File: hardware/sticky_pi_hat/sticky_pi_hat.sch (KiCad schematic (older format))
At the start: 28 parts, among them J1 Screw_Terminal_01x11, J2 Conn_02x13_Odd_Even, J3 Conn_01x02_Male, Q1 BSS806NH6327XTSA1, SW1 SW_Push, U1 DHT22, U2 TPL5110, U3 TPS63002, U4 DS1307Z+, Y1 Crystal

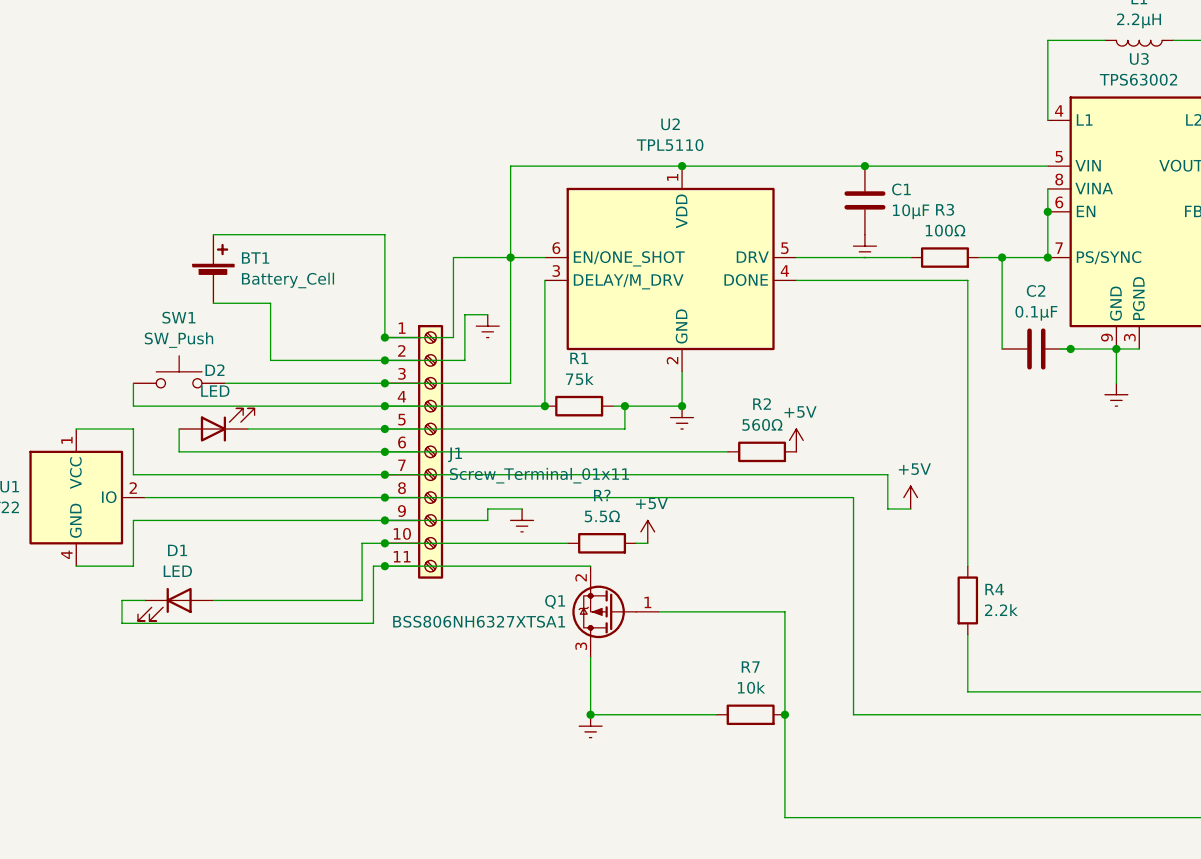
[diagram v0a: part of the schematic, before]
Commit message: Add P-channel mosfet to tpl5110
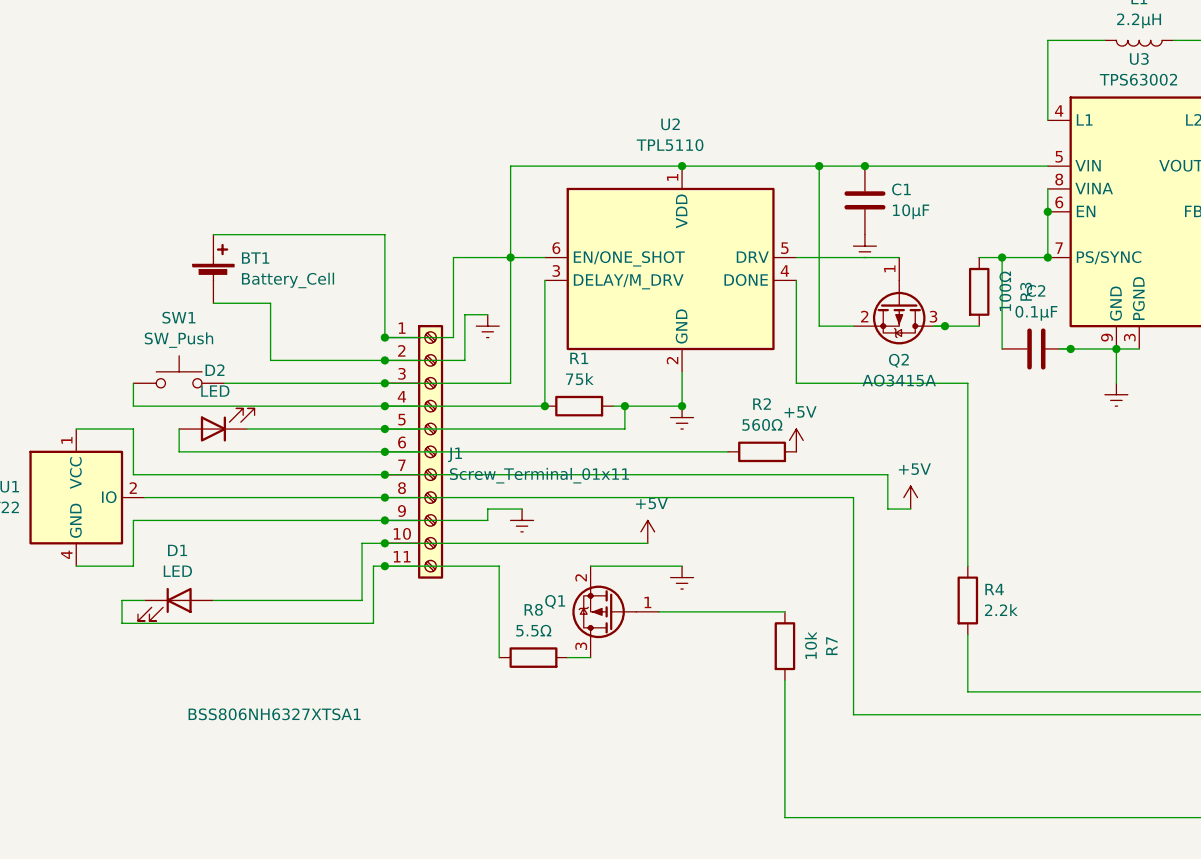
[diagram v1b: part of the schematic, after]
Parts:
- added Q2: AO3415A, Package_TO_SOT_SMD:SOT-23, symbol Transistor_FET:BSS84
- Q1: part_number SI2319CDS-T1-GE3 -> BSS806NH6327XTSA1
- gave numbers to parts that had none: 1
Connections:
- wire segments 129 -> 134
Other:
- moved on the sheet: R3, R7, R8
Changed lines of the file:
@@
 L Device:R R3
 U 1 1 613829B2
-P 5450 2650
-F 0 "R3" V 5657 2650 50  0000 C CNN
-F 1 "100Ω" V 5566 2650 50  0000 C CNN
-F 2 "Resistor_SMD:R_2010_5025Metric" V 5380 2650 50  0001 C CNN
-F 3 "https://www.koaspeer.com/pdfs/RK73H.pdf" H 5450 2650 50  0001 C CNN
-F 4 "RC2010JK-0710KL" H 5450 2650 50  0001 C CNN "part_number"
-F 5 "KOA Speer Electronics, Inc." H 5450 2650 50  0001 C CNN "Manufacturer"
-F 6 "" H 5450 2650 50  0001 C CNN "Vendor"
-F 7 "RC2010JK-0710KL" H 5450 2650 50  0001 C CNN "Part"
-	1    5450 2650
-	0    -1   -1   0
+P 5600 2800
+F 0 "R3" V 5807 2800 50  0000 C CNN
+F 1 "100Ω" V 5716 2800 50  0000 C CNN
+F 2 "Resistor_SMD:R_2010_5025Metric" V 5530 2800 50  0001 C CNN
+F 3 "https://www.koaspeer.com/pdfs/RK73H.pdf" H 5600 2800 50  0001 C CNN
+F 4 "RC2010JK-0710KL" H 5600 2800 50  0001 C CNN "part_number"
+F 5 "KOA Speer Electronics, Inc." H 5600 2800 50  0001 C CNN "Manufacturer"
+F 6 "" H 5600 2800 50  0001 C CNN "Vendor"
+F 7 "RC2010JK-0710KL" H 5600 2800 50  0001 C CNN "Part"
+	1    5600 2800
+	1    0    0    -1
 $EndComp
 $Comp
@@
 	1    0    0    -1
 $EndComp
-$Comp
-L Device:C C1
-U 1 1 613C0503
-P 5100 2400
-F 0 "C1" H 5215 2446 50  0000 L CNN
-F 1 "10μF" H 5215 2355 50  0000 L CNN
-F 2 "Capacitor_SMD:C_1206_3216Metric" H 5138 2250 50  0001 C CNN
-F 3 "https://global.kyocera.com/prdct/electro/product/pdf/cm_e.pdf" H 5100 2400 50  0001 C CNN
-F 4 "CM316X5R106K10AT" H 5100 2400 50  0001 C CNN "part_number"
-F 5 "Kyocera International Inc. Electronic Components" H 5100 2400 50  0001 C CNN "Manufacturer"
-F 6 "" H 5100 2400 50  0001 C CNN "Vendor"
-F 7 "CM316X5R106K10AT" H 5100 2400 50  0001 C CNN "Part"
-	1    5100 2400
-	1    0    0    -1
-$EndComp
 Wire Wire Line
 	5600 2650 5700 2650
@@
 Wire Wire Line
 	6000 3050 6200 3050
-$Comp
-L power:Earth #PWR0103
-U 1 1 613C9F6B
-P 5100 2550
-F 0 "#PWR0103" H 5100 2300 50  0001 C CNN
-F 1 "Earth" H 5100 2400 50  0001 C CNN
-F 2 "" H 5100 2550 50  0001 C CNN
-F 3 "~" H 5100 2550 50  0001 C CNN
-	1    5100 2550
-	1    0    0    -1
-$EndComp
 Wire Wire Line
 	6700 2450 6700 2250
@@
 	1    0    0    -1
 $EndComp
-Wire Wire Line
-	3000 4000 3900 4000
 $Comp
 L power:Earth #PWR0108
 U 1 1 615E52C8
-P 3900 4650
-F 0 "#PWR0108" H 3900 4400 50  0001 C CNN
-F 1 "Earth" H 3900 4500 50  0001 C CNN
-F 2 "" H 3900 4650 50  0001 C CNN
-F 3 "~" H 3900 4650 50  0001 C CNN
-	1    3900 4650
+P 4300 4000
+F 0 "#PWR0108" H 4300 3750 50  0001 C CNN
+F 1 "Earth" H 4300 3850 50  0001 C CNN
+F 2 "" H 4300 4000 50  0001 C CNN
+F 3 "~" H 4300 4000 50  0001 C CNN
+	1    4300 4000
 	1    0    0    -1
 $EndComp
@@
 	7250 2250 7300 2250
 Wire Wire Line
-	4750 4650 4750 4200
-Wire Wire Line
 	3000 4000 2950 4000
-Connection ~ 3000 4000
 Wire Wire Line
 	3000 3900 2900 3900
-Connection ~ 3000 3900
 Wire Wire Line
 	3000 3700 5050 3700
@@
 P 4000 4200
 F 0 "Q1" H 4205 4154 50  0000 L CNN
-F 1 "BSS806NH6327XTSA1" H 4205 4245 50  0000 L CNN
+F 1 "BSS806NH6327XTSA1" H 5100 4650 50  0000 L CNN
 F 2 "Package_TO_SOT_SMD:SOT-23" H 4200 4125 50  0001 L CIN
 F 3 "https://www.infineon.com/dgdl/BSS806N_Rev2.3_.pdf?folderId=db3a3043156fd573011622e10b5c1f67&fileId=db3a304330f686060131185f0553451c" H 4000 4200 50  0001 L CNN
 F 4 "Infineon Technologies" H 4000 4200 50  0001 C CNN "Manufacturer"
-F 5 "SI2319CDS-T1-GE3" H 4000 4200 50  0001 C CNN "part_number"
+F 5 "BSS806NH6327XTSA1" H 4000 4200 50  0001 C CNN "part_number"
 F 6 "" H 4000 4200 50  0001 C CNN "Vendor"
 F 7 "BSS806NH6327XTSA1" H 4000 4200 50  0001 C CNN "Part"
@@
 L Device:R R7
 U 1 1 61A13B53
-P 4600 4650
-F 0 "R7" V 4807 4650 50  0000 C CNN
-F 1 "10k" V 4716 4650 50  0000 C CNN
-F 2 "Resistor_SMD:R_2010_5025Metric" V 4530 4650 50  0001 C CNN
-F 3 "https://www.yageo.com/upload/media/product/productsearch/datasheet/rchip/PYu-RC_Group_51_RoHS_L_11.pdf" H 4600 4650 50  0001 C CNN
-F 4 "RC2010JK-0710KL" H 4600 4650 50  0001 C CNN "part_number"
-F 5 "YAGEO" H 4600 4650 50  0001 C CNN "Manufacturer"
-F 6 "" H 4600 4650 50  0001 C CNN "Vendor"
-F 7 "RC2010JK-0710KL" H 4600 4650 50  0001 C CNN "Part"
-	1    4600 4650
-	0    -1   -1   0
+P 4750 4350
+F 0 "R7" V 4957 4350 50  0000 C CNN
+F 1 "10k" V 4866 4350 50  0000 C CNN
+F 2 "Resistor_SMD:R_2010_5025Metric" V 4680 4350 50  0001 C CNN
+F 3 "https://www.yageo.com/upload/media/product/productsearch/datasheet/rchip/PYu-RC_Group_51_RoHS_L_11.pdf" H 4750 4350 50  0001 C CNN
+F 4 "RC2010JK-0710KL" H 4750 4350 50  0001 C CNN "part_number"
+F 5 "YAGEO" H 4750 4350 50  0001 C CNN "Manufacturer"
+F 6 "" H 4750 4350 50  0001 C CNN "Vendor"
+F 7 "RC2010JK-0710KL" H 4750 4350 50  0001 C CNN "Part"
+	1    4750 4350
+	1    0    0    -1
 $EndComp
 Wire Wire Line
 	4750 4200 4200 4200
 Wire Wire Line
-	3900 4400 3900 4650
-Wire Wire Line
-	4450 4650 3900 4650
-Connection ~ 3900 4650
-Wire Wire Line
 	7900 4150 7900 4250
 Wire Wire Line
@@
 Wire Wire Line
 	5050 3700 5050 4650
-Wire Wire Line
-	4750 5100 4750 4650
-Connection ~ 4750 4650
 Connection ~ 5100 2250
-Wire Wire Line
-	5100 2250 4300 2250
-Wire Wire Line
-	4800 2650 5300 2650
 $Comp
 L power:+5V #PWR0113
@@
 	1    0    0    -1
 $EndComp
-Wire Wire Line
-	5550 2750 4800 2750
-Wire Wire Line
-	5550 2750 5550 4000
 Wire Wire Line
 	8100 3500 8100 4050
@@
 	7950 4650 5050 4650
 $Comp
-L Device:R R?
+L Device:R R8
 U 1 1 614F2EDD
-P 3950 3900
-F 0 "R?" V 4157 3900 50  0000 C CNN
-F 1 "5.5Ω" V 4066 3900 50  0000 C CNN
-F 2 "Resistor_SMD:R_2010_5025Metric" V 3880 3900 50  0001 C CNN
-F 3 "https://www.yageo.com/upload/media/product/productsearch/datasheet/rchip/PYu-AC_51_RoHS_L_7.pdf" H 3950 3900 50  0001 C CNN
-F 4 "AC2010JK-07560RL" H 3950 3900 50  0001 C CNN "part_number"
-F 5 "YAGEO" H 3950 3900 50  0001 C CNN "Manufacturer"
-F 6 "" H 3950 3900 50  0001 C CNN "Vendor"
-F 7 "AC2010JK-07560RL" H 3950 3900 50  0001 C CNN "Part"
-	1    3950 3900
+P 3650 4400
+F 0 "R8" V 3857 4400 50  0000 C CNN
+F 1 "5.5Ω" V 3766 4400 50  0000 C CNN
+F 2 "Resistor_SMD:R_2010_5025Metric" V 3580 4400 50  0001 C CNN
+F 3 "https://www.yageo.com/upload/media/product/productsearch/datasheet/rchip/PYu-AC_51_RoHS_L_7.pdf" H 3650 4400 50  0001 C CNN
+F 4 "AC2010JK-07560RL" H 3650 4400 50  0001 C CNN "part_number"
+F 5 "YAGEO" H 3650 4400 50  0001 C CNN "Manufacturer"
+F 6 "" H 3650 4400 50  0001 C CNN "Vendor"
+F 7 "AC2010JK-07560RL" H 3650 4400 50  0001 C CNN "Part"
+	1    3650 4400
 	0    -1   -1   0
 $EndComp
 Wire Wire Line
-	3000 3900 3800 3900
-Wire Wire Line
-	4150 3900 4100 3900
+	4750 4500 4750 5100
+Wire Wire Line
+	3900 4000 4300 4000
+Wire Wire Line
+	3800 4400 3900 4400
+Connection ~ 3000 4000
+Wire Wire Line
+	3500 4400 3500 4000
+Wire Wire Line
+	3500 4000 3000 4000
+Connection ~ 3000 3900
+Wire Wire Line
+	3000 3900 4150 3900
+Wire Wire Line
+	4800 2750 4800 3200
+Wire Wire Line
+	4800 3200 5550 3200
+Wire Wire Line
+	5550 3200 5550 4000
+$Comp
+L power:Earth #PWR0103
+U 1 1 613C9F6B
+P 5100 2550
+F 0 "#PWR0103" H 5100 2300 50  0001 C CNN
+F 1 "Earth" H 5100 2400 50  0001 C CNN
+F 2 "" H 5100 2550 50  0001 C CNN
+F 3 "~" H 5100 2550 50  0001 C CNN
+	1    5100 2550
+	1    0    0    -1
+$EndComp
+Wire Wire Line
+	5100 2250 4900 2250
+$Comp
+L Device:C C1
+U 1 1 613C0503
+P 5100 2400
+F 0 "C1" H 5215 2446 50  0000 L CNN
+F 1 "10μF" H 5215 2355 50  0000 L CNN
+F 2 "Capacitor_SMD:C_1206_3216Metric" H 5138 2250 50  0001 C CNN
+F 3 "https://global.kyocera.com/prdct/electro/product/pdf/cm_e.pdf" H 5100 2400 50  0001 C CNN
+F 4 "CM316X5R106K10AT" H 5100 2400 50  0001 C CNN "part_number"
+F 5 "Kyocera International Inc. Electronic Components" H 5100 2400 50  0001 C CNN "Manufacturer"
+F 6 "" H 5100 2400 50  0001 C CNN "Vendor"
+F 7 "CM316X5R106K10AT" H 5100 2400 50  0001 C CNN "Part"
+	1    5100 2400
+	1    0    0    -1
+$EndComp
+Connection ~ 4900 2250
+Wire Wire Line
+	4900 2250 4300 2250
+$Comp
+L Transistor_FET:BSS84 Q2
+U 1 1 6167A20B
+P 5250 2850
+F 0 "Q2" V 5499 2850 50  0000 C CNN
+F 1 "AO3415A" V 5590 2850 50  0000 C CNN
+F 2 "Package_TO_SOT_SMD:SOT-23" H 5450 2775 50  0001 L CIN
+F 3 "https://media.digikey.com/pdf/Data%20Sheets/Alpha%20&%20Omega/AO3415A.pdf" H 5250 2850 50  0001 L CNN
+F 4 "Alpha & Omega Semiconductor Inc." H 5250 2850 50  0001 C CNN "Manufacturer"
+F 5 "AO3415A" H 5250 2850 50  0001 C CNN "Part"
+F 6 "AO3415A" H 5250 2850 50  0001 C CNN "part_number"
+	1    5250 2850
+	0    1    1    0
+$EndComp
+Wire Wire Line
+	5600 2950 5450 2950
+Connection ~ 5450 2950
+Wire Wire Line
+	5450 2950 5400 2950
+Wire Wire Line
+	4800 2650 5250 2650
+Wire Wire Line
+	5050 2950 4900 2950
+Wire Wire Line
+	4900 2250 4900 2950
 $EndSCHEMATC

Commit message: update
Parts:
- added C6: 10μF, Capacitor_SMD:C_1206_3216Metric, symbol Device:C
- added D3: SM4001PL, Diode_SMD:D_SOD-123F, symbol Diode:SM4001
- added Q3, Q4: BSS806NH6327XTSA1, Package_TO_SOT_SMD:SOT-23, symbol Transistor_FET:BSS123
- added R10: 75k, Resistor_SMD:R_2010_5025Metric, symbol Device:R
- added R9: 49.9k, Resistor_SMD:R_0805_2012Metric, symbol Device:R
- added U5: MCP3001-I_ST, Microchip-MCP3001-I_ST-*:Microchip-MCP3001-I_ST-Level_A, symbol 3001:MCP3001-I_ST
- D1, J1, J3, SW1, U1: Manufacturer (none) -> #none; Part (none) -> #none
- D2: Manufacturer (none) -> #none; Part (none) -> WP7113SECK/J3
- J2: Part 1-215307-0 -> 1-215307-3
- Q1: symbol Transistor_FET:Si2319CDS -> Transistor_FET:BSS123
- R8: Part AC2010JK-07560RL -> RC2010FK-075R49L; part_number AC2010JK-07560RL -> RC2010FK-075R49L
- U2: Part TPL5110 -> TPL5110QDDCTQ1; part_number TPL5110 -> TPL5110QDDCTQ1
- U3: Part TPS63002 -> TPS63002DRCR; part_number TPS63002 -> TPS63002DRCR
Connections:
- net labels added: +BATT, GPIO_11_clk, GPIO_17_R, GPIO_2, GPIO_22, GPIO_23, GPIO_27, GPIO_3, GPIO_8_C0, GPIO_9_MISO, drv, push_button
- wire segments 134 -> 108
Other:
- note added: "Battery Level ADC Reader"
- note added: "Button State Holder"
- note added: "RTC\n"
- note added: "Raspberry Pi Pins\n"
- note added: "Wake Up Timer"
- moved on the sheet: BT1, BT2, C1, C2, C3, C4, C5, D1, J2, J3, L1, Q1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

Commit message: add external pull down resistor to flash and push button outputs
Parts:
- added C7: 47uF, Capacitor_SMD:CP_Elec_5x5.3, symbol Device:CP1
- added R11, R12: 10k, Resistor_SMD:R_2010_5025Metric, symbol Device:R
- J2: part_number 1-215307-0 -> 1-215307-3
- U2: Part TPL5110QDDCTQ1 -> TPL5110; part_number TPL5110QDDCTQ1 -> TPL5110
- U3: Part TPS63002DRCR -> TPS63002; part_number TPS63002DRCR -> TPS63002
- U4: part_number DS1307+ -> DS1307Z+
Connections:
- net labels added: batt_io
- wire segments 108 -> 117
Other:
- moved on the sheet: R10, R4, R9
